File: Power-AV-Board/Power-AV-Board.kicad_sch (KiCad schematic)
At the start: 69 parts, among them IC502 NJM2360AD, J501A Yellow, J501B White, J501C Red Switched, J502 Barrel Jack, J503 CB, J504 CC, Q501 2SC1740, U1 NJM2246

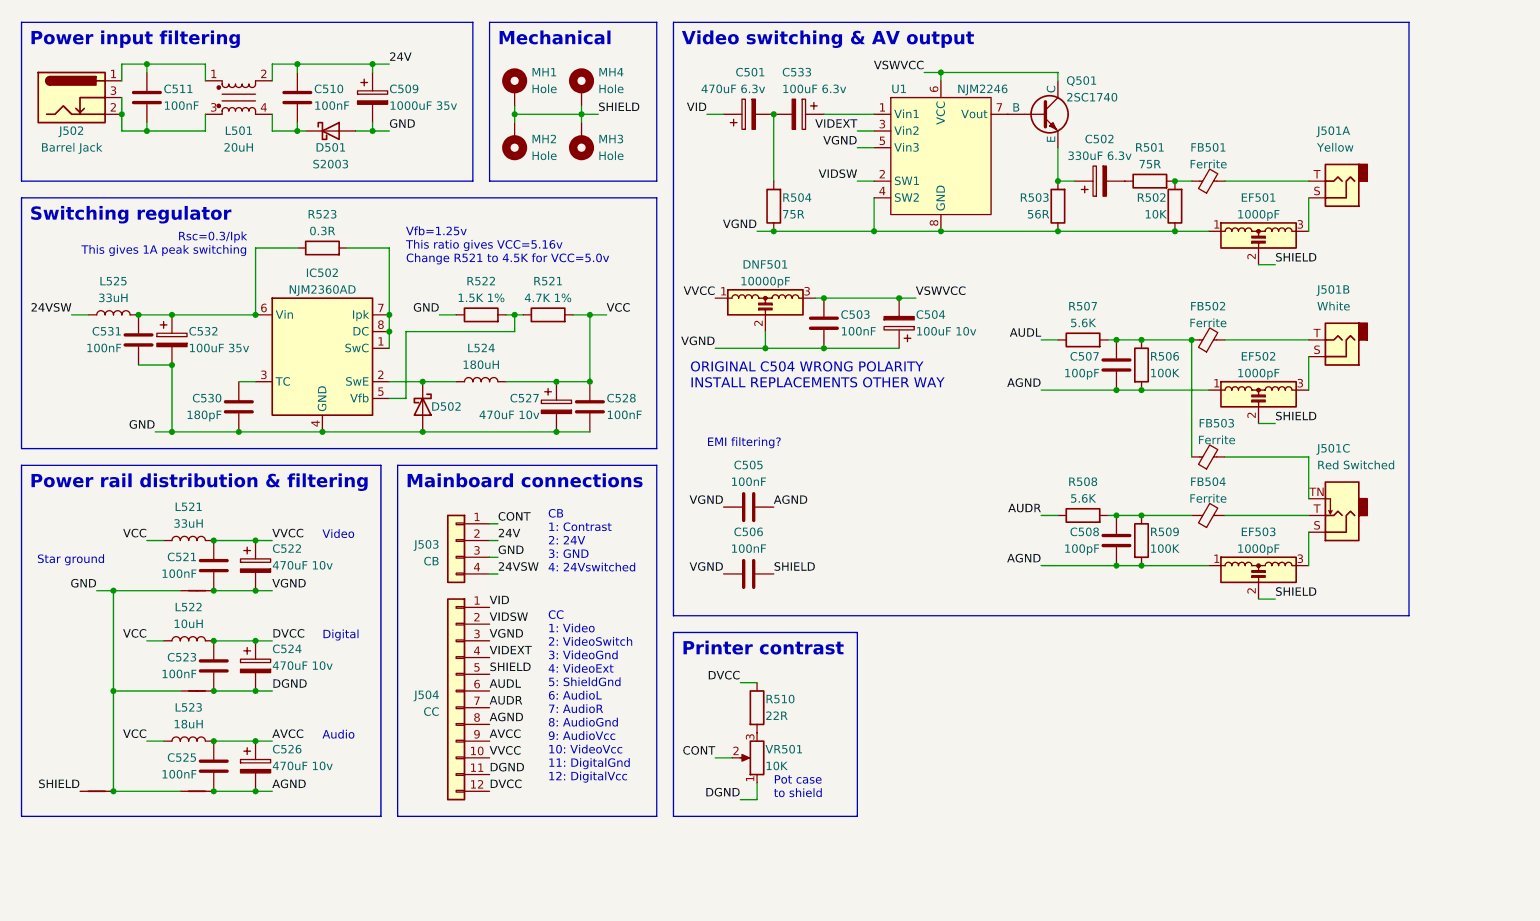
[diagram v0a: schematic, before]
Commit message: Update all to Kicad 9.0 and cleanup
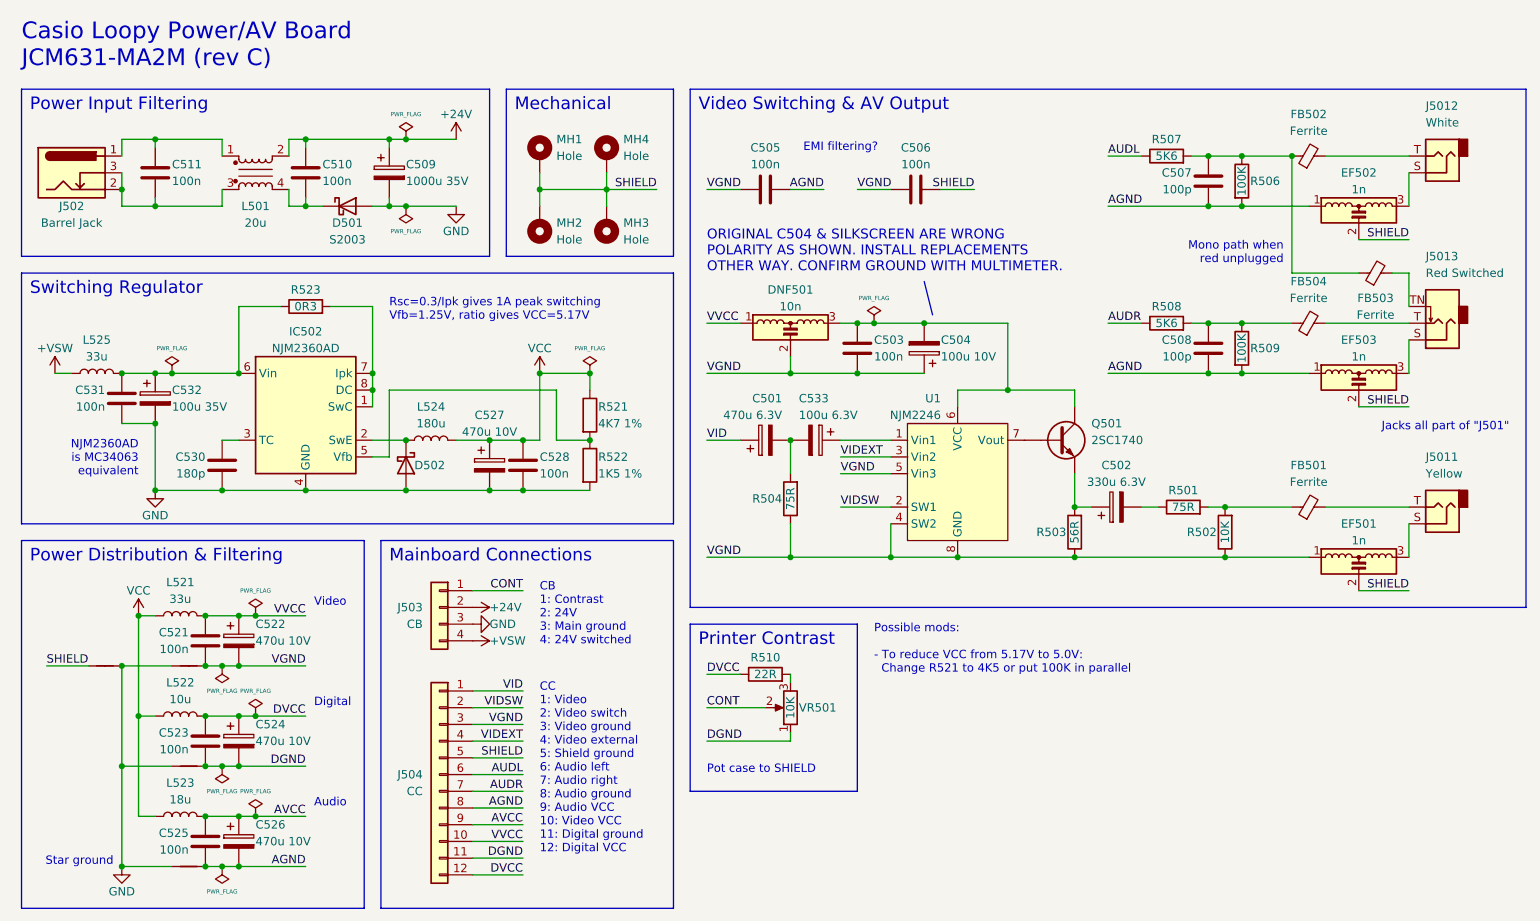
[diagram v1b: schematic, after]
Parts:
- removed Q501: 2SC1740, symbol Simulation_SPICE:NPN
- added Q501: 2SC1740, symbol Device:Q_NPN
- C501: value 470uF 6.3v -> 470u 6.3V
- C502: value 330uF 6.3v -> 330u 6.3V
- C503, C505, C506, C510, C511, C521, C523, C525, C528, C531: value 100nF -> 100n
- C504: value 100uF 10v -> 100u 10V
- C507, C508: value 100pF -> 100p
- C509: value 1000uF 35v -> 1000u 35V
- C522, C524, C526, C527: value 470uF 10v -> 470u 10V
- C530: value 180pF -> 180p
- C532: value 100uF 35v -> 100u 35V
- C533: value 100uF 6.3v -> 100u 6.3V
- DNF501: value 10000pF -> 10n
- EF501, EF502, EF503: value 1000pF -> 1n
- L501: value 20uH -> 20u
- L521, L525: value 33uH -> 33u
- L522: value 10uH -> 10u
- L523: value 18uH -> 18u
- L524: value 180uH -> 180u
- R507, R508: value 5.6K -> 5K6
- R521: value 4.7K 1% -> 4K7 1%
- R522: value 1.5K 1% -> 1K5 1%
- R523: value 0.3R -> 0R3
- U1: symbol _project_parts:NJM2246 -> project_parts:NJM2246
- renumbered J501A to J5011, J501B to J5012, J501C to J5013
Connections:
- net GND: now also R522.2; no longer R522.1
- net VCC: now also R521.1; no longer R521.2
- net at U1.7 (Vout): now also Q501.B
- net at C502.1, R503.2: now also Q501.E
- net 24V renamed +24V
- net 24VSW renamed +VSW
- net VSWVCC: no longer names the net of C503.1, C504.2, DNF501.3, U1.6 (VCC)
- net VSWVCC: now also Q501.C
- new net: IC502.5 (Vfb), R521.2, R522.1
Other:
- note added: "CB 1: Contrast 2: 24V 3: Main ground 4: 24V switched"
- note added: "CC 1: Video 2: Video switch 3: Video ground 4: Video external 5: Shield ground 6: Audio left 7: Audio right 8: Audio ground 9: Audio VCC 10: Video VCC 11: Digital ground 12: Digital VCC"
- note added: "Casio Loopy Power/AV Board JCM631-MA2M (rev C)"
- note added: "Jacks all part of "J501""
- note added: "Mainboard Connections"
- note added: "Mono path when red unplugged"
- note added: "NJM2360AD is MC34063 equivalent"
- note added: "ORIGINAL C504 & SILKSCREEN ARE WRONG POLARITY AS SHOWN. INSTALL REPLACEMENTS OTHER WAY. CONFIRM GROUND WITH MULTIMETER."
- note added: "Possible mods: - To reduce VCC from 5.17V to 5.0V: Change R521 to 4K5 or put 100K in parallel"
- note added: "Pot case to SHIELD"
- note added: "Power Distribution & Filtering"
- note added: "Power Input Filtering"
- note added: "Printer Contrast"
- note added: "Rsc=0.3/Ipk gives 1A peak switching Vfb=1.25V, ratio gives VCC=5.17V"
- note added: "Switching Regulator"
- note added: "Video Switching & AV Output"
- note removed: "CB 1: Contrast 2: 24V 3: GND 4: 24Vswitched"
- note removed: "CC 1: Video 2: VideoSwitch 3: VideoGnd 4: VideoExt 5: ShieldGnd 6: AudioL 7: AudioR 8: AudioGnd 9: AudioVcc 10: VideoVcc 11: DigitalGnd 12: DigitalVcc"
- note removed: "Mainboard connections"
- note removed: "ORIGINAL C504 WRONG POLARITY INSTALL REPLACEMENTS OTHER WAY"
- note removed: "Pot case to shield"
- note removed: "Power input filtering"
- note removed: "Power rail distribution & filtering"
- note removed: "Printer contrast"
- note removed: "Rsc=0.3/Ipk This gives 1A peak switching"
- note removed: "Switching regulator"
- note removed: "Vfb=1.25v This ratio gives VCC=5.16v Change R521 to 4.5K for VCC=5.0v"
- note removed: "Video switching & AV output"
- moved on the sheet: C501, C502, C503, C504, C505, C506, C507, C508, C509, C510, C511, C521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

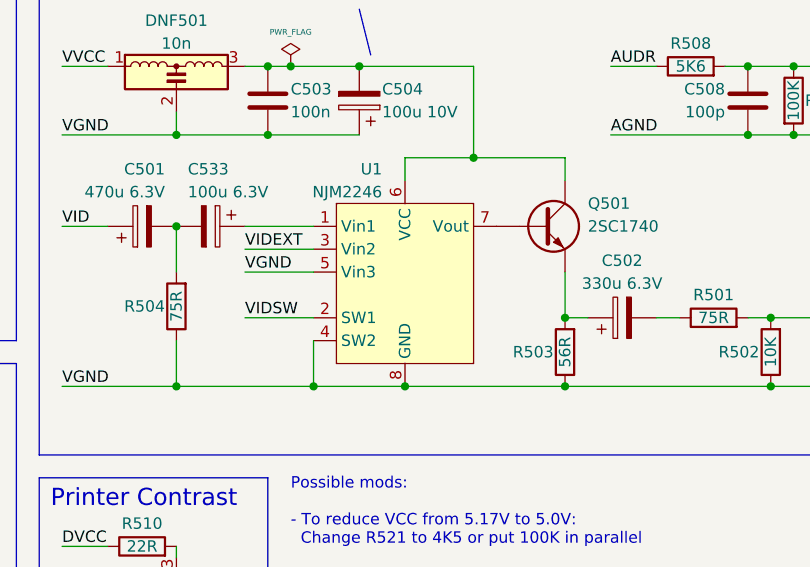
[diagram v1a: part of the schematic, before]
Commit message: Unify project part libs
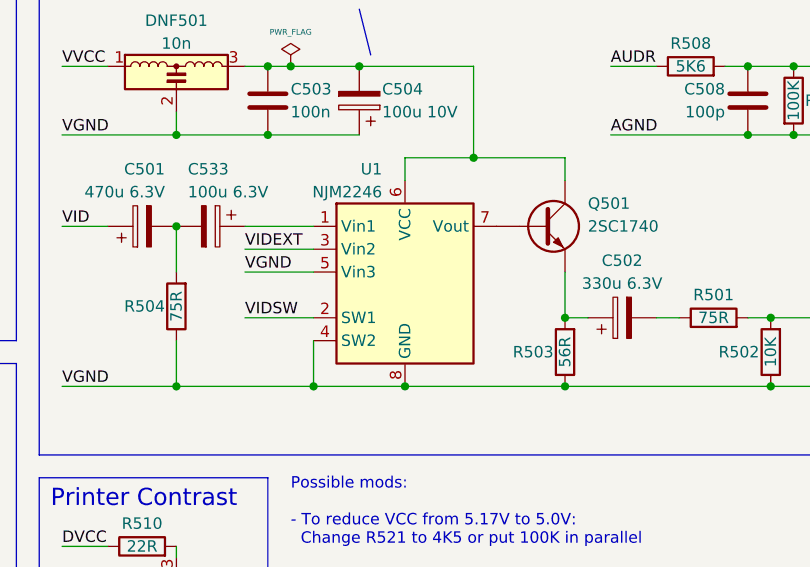
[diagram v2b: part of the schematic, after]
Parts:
- U1: symbol project_parts:NJM2246 -> loopy-parts:NJM2246
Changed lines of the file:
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@@
 	)
 	(symbol
-		(lib_id "project_parts:NJM2246")
+		(lib_id "loopy-parts:NJM2246")
 		(at 157.48 85.09 0)
 		(unit 1)

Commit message: Render current schematics to PDF
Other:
- title: Casio Loopy IO Board -> (none)
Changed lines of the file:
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@@
 	(paper "A4")
 	(title_block
-		(title "Casio Loopy IO Board")
-		(rev "MA2MC")
+		(comment 3 "github.com/kasamikona/Loopy-Schematics")
+		(comment 4 "Reverse-engineered by Kasami with help from the Loopy community")
 	)
 	(rectangle
